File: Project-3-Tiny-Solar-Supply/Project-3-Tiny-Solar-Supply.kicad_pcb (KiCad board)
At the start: 2 copper layers, 40.8 x 18.5 mm, 16 parts, among them J1 Conn_01x02_Pin, J2 Conn_01x02_Pin, J3 Conn_01x02_Pin, J4 Conn_01x02_Pin, Q1 2N7002, U1 AP3015AKTR-G1

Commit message: rotate diodes
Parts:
- turned D1 to 180 degrees
- turned D2 to 180 degrees
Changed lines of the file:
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@@
 	(footprint "SS14:DO-214AC"
 		(layer "F.Cu")
-		(at 58.75 86)
+		(at 58.75 86 180)
 		(property "Reference" "D1"
-			(at 4.05 0.1 0)
+			(at -4.15 0.1 0)
 			(layer "F.SilkS")
 			(effects
@@
 		(duplicate_pad_numbers_are_jumpers no)
 		(fp_line
+			(start 2.3 1.2)
+			(end -2.3 1.2)
+			(stroke
+				(width 0.15)
+				(type solid)
+			)
+			(layer "F.SilkS")
+		)
+		(fp_line
+			(start 0.25 0.7)
+			(end -0.8 0)
+			(stroke
+				(width 0.15)
+				(type solid)
+			)
+			(layer "F.SilkS")
+		)
+		(fp_line
+			(start 0.25 -0.75)
+			(end 0.25 0.7)
+			(stroke
+				(width 0.15)
+				(type solid)
+			)
+			(layer "F.SilkS")
+		)
+		(fp_line
+			(start -0.8 0)
+			(end 0.25 -0.75)
+			(stroke
+				(width 0.15)
+				(type solid)
+			)
+			(layer "F.SilkS")
+		)
+		(fp_line
 			(start -2.3 -1.2)
 			(end 2.3 -1.2)
-			(stroke
-				(width 0.15)
-				(type solid)
-			)
-			(layer "F.SilkS")
-		)
-		(fp_line
-			(start -0.8 0)
-			(end 0.25 -0.75)
-			(stroke
-				(width 0.15)
-				(type solid)
-			)
-			(layer "F.SilkS")
-		)
-		(fp_line
-			(start 0.25 -0.75)
-			(end 0.25 0.7)
-			(stroke
-				(width 0.15)
-				(type solid)
-			)
-			(layer "F.SilkS")
-		)
-		(fp_line
-			(start 0.25 0.7)
-			(end -0.8 0)
-			(stroke
-				(width 0.15)
-				(type solid)
-			)
-			(layer "F.SilkS")
-		)
-		(fp_line
-			(start 2.3 1.2)
-			(end -2.3 1.2)
 			(stroke
 				(width 0.15)
@@
 		)
 		(fp_line
+			(start 2.3 -1.2)
+			(end 2.3 1.2)
+			(stroke
+				(width 0.15)
+				(type solid)
+			)
+			(layer "F.Fab")
+		)
+		(fp_line
 			(start -2.3 1.2)
 			(end -2.3 -1.2)
@@
 			(layer "F.Fab")
 		)
-		(fp_line
-			(start 2.3 -1.2)
-			(end 2.3 1.2)
-			(stroke
-				(width 0.15)
-				(type solid)
-			)
+		(fp_poly
+			(pts
+				(xy 2.35 -0.65) (xy 2.6 -0.65) (xy 2.6 0.7) (xy 2.35 0.7)
+			)
+			(stroke
+				(width 0.01)
+				(type solid)
+			)
+			(fill yes)
 			(layer "F.Fab")
 		)
@@
 			(layer "F.Fab")
 		)
-		(fp_poly
-			(pts
-				(xy 2.35 -0.65) (xy 2.6 -0.65) (xy 2.6 0.7) (xy 2.35 0.7)
-			)
-			(stroke
-				(width 0.01)
-				(type solid)
-			)
-			(fill yes)
-			(layer "F.Fab")
-		)
 		(pad "A" smd rect
-			(at 2.05 0)
+			(at 2.05 0 180)
 			(size 1.8 1.7)
 			(layers "F.Cu" "F.Mask" "F.Paste")
@@
 		)
 		(pad "K" smd rect
-			(at -2.05 0)
+			(at -2.05 0 180)
 			(size 1.8 1.7)
 			(layers "F.Cu" "F.Mask" "F.Paste")
@@
 	(footprint "SS14:DO-214AC"
 		(layer "F.Cu")
-		(at 49.5 86)
+		(at 49.5 86 180)
 		(property "Reference" "D2"
-			(at 4.1 0.1 0)
+			(at -4.1 0.1 0)
 			(layer "F.SilkS")
 			(effects
@@
 		(duplicate_pad_numbers_are_jumpers no)
 		(fp_line
+			(start 2.3 1.2)
+			(end -2.3 1.2)
+			(stroke
+				(width 0.15)
+				(type solid)
+			)
+			(layer "F.SilkS")
+		)
+		(fp_line
+			(start 0.25 0.7)
+			(end -0.8 0)
+			(stroke
+				(width 0.15)
+				(type solid)
+			)
+			(layer "F.SilkS")
+		)
+		(fp_line
+			(start 0.25 -0.75)
+			(end 0.25 0.7)
+			(stroke
+				(width 0.15)
+				(type solid)
+			)
+			(layer "F.SilkS")
+		)
+		(fp_line
+			(start -0.8 0)
+			(end 0.25 -0.75)
+			(stroke
+				(width 0.15)
+				(type solid)
+			)
+			(layer "F.SilkS")
+		)
+		(fp_line
 			(start -2.3 -1.2)
 			(end 2.3 -1.2)
-			(stroke
-				(width 0.15)
-				(type solid)
-			)
-			(layer "F.SilkS")
-		)
-		(fp_line
-			(start -0.8 0)
-			(end 0.25 -0.75)
-			(stroke
-				(width 0.15)
-				(type solid)
-			)
-			(layer "F.SilkS")
-		)
-		(fp_line
-			(start 0.25 -0.75)
-			(end 0.25 0.7)
-			(stroke
-				(width 0.15)
-				(type solid)
-			)
-			(layer "F.SilkS")
-		)
-		(fp_line
-			(start 0.25 0.7)
-			(end -0.8 0)
-			(stroke
-				(width 0.15)
-				(type solid)
-			)
-			(layer "F.SilkS")
-		)
-		(fp_line
-			(start 2.3 1.2)
-			(end -2.3 1.2)
 			(stroke
 				(width 0.15)
@@
 		)
 		(fp_line
+			(start 2.3 -1.2)
+			(end 2.3 1.2)
+			(stroke
+				(width 0.15)
+				(type solid)
+			)
+			(layer "F.Fab")
+		)
+		(fp_line
 			(start -2.3 1.2)
 			(end -2.3 -1.2)
@@
 			(layer "F.Fab")
 		)
-		(fp_line
-			(start 2.3 -1.2)
-			(end 2.3 1.2)
-			(stroke
-				(width 0.15)
-				(type solid)
-			)
+		(fp_poly
+			(pts
+				(xy 2.35 -0.65) (xy 2.6 -0.65) (xy 2.6 0.7) (xy 2.35 0.7)
+			)
+			(stroke
+				(width 0.01)
+				(type solid)
+			)
+			(fill yes)
 			(layer "F.Fab")
 		)
@@
 			(layer "F.Fab")
 		)
-		(fp_poly
-			(pts
-				(xy 2.35 -0.65) (xy 2.6 -0.65) (xy 2.6 0.7) (xy 2.35 0.7)
-			)
-			(stroke
-				(width 0.01)
-				(type solid)
-			)
-			(fill yes)
-			(layer "F.Fab")
-		)
 		(pad "A" smd rect
-			(at 2.05 0)
+			(at 2.05 0 180)
 			(size 1.8 1.7)
 			(layers "F.Cu" "F.Mask" "F.Paste")
@@
 		)
 		(pad "K" smd rect
-			(at -2.05 0)
+			(at -2.05 0 180)
 			(size 1.8 1.7)
 			(layers "F.Cu" "F.Mask" "F.Paste")

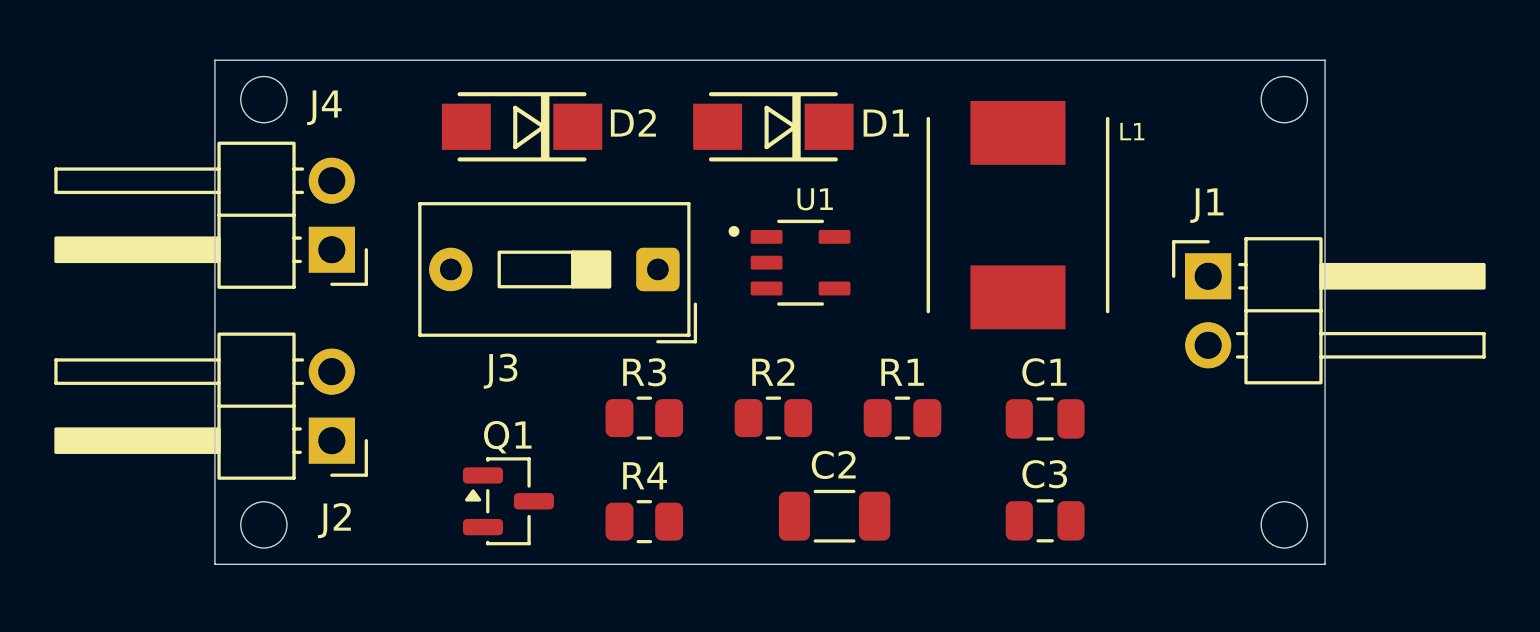
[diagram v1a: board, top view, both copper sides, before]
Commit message: re-arrange and wire footprints (GND plane missing)
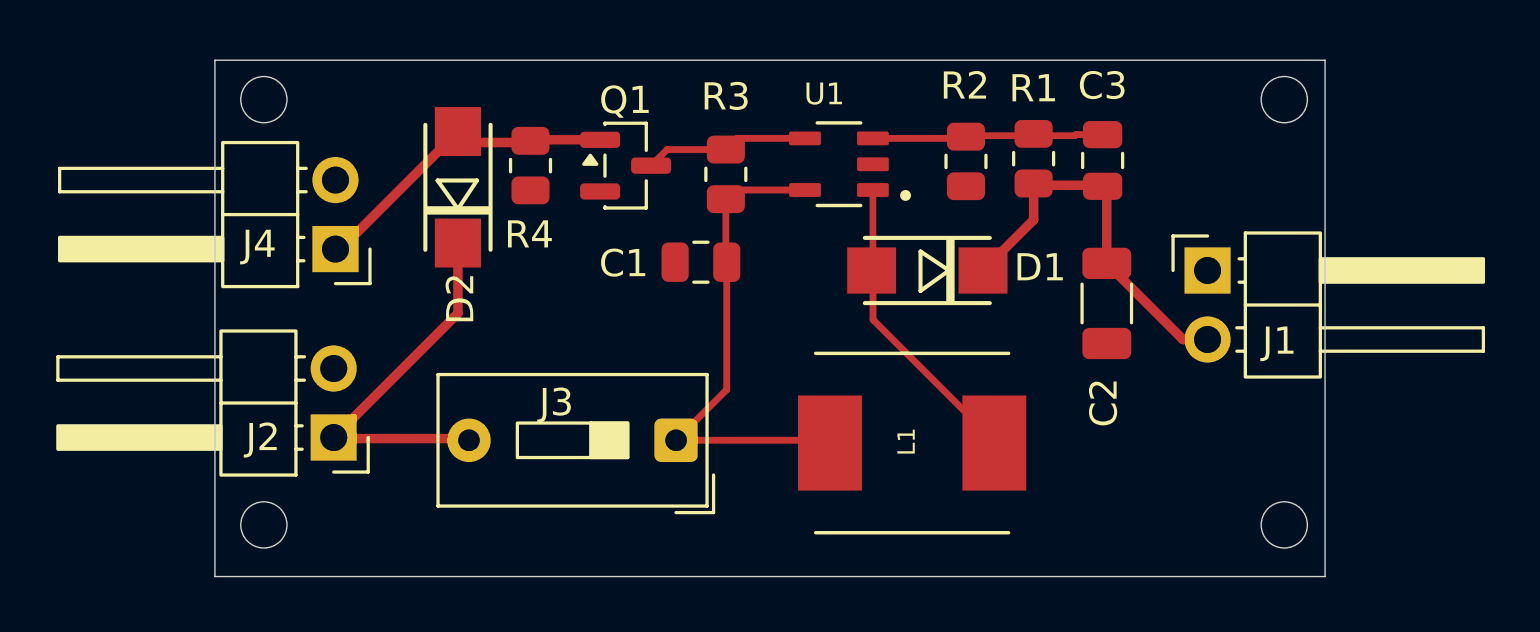
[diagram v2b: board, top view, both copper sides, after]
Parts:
- moved C1 13.9 mm to (56.1, 91.0), turned to 180 degrees
- moved R4 13.8 mm to (49.8, 87.4), turned to -90 degrees
- moved C3 13.4 mm to (70.9, 87.2), turned to 90 degrees
- moved Q1 13.1 mm to (53.3, 87.4)
- moved C2 12.7 mm to (71.0, 92.5), turned to -90 degrees
- moved R2 11.8 mm to (65.8, 87.3), turned to -90 degrees
- moved R1 10.7 mm to (68.3, 87.2), turned to 90 degrees
- moved R3 9.46 mm to (57.0, 87.8), turned to 90 degrees
- moved L1 9.25 mm to (63.9, 97.6), turned to 0 degrees
- moved D1 7.75 mm to (64.4, 91.3)
- moved J3 6.32 mm to (55.2, 97.5)
- moved U1 3.89 mm to (61.2, 87.4), turned to 180 degrees
- moved D2 3.24 mm to (47.1, 88.2), turned to 90 degrees
- moved J1 0.21 mm to (74.7, 91.3)
- moved J4 0.14 mm to (42.6, 90.5)
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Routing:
- net Net-(J3-Pin_1): track 0.00 -> 18.0 mm
- net /OUT_P: track 0.00 -> 14.8 mm
- net /BAT_P: track 0.00 -> 14.1 mm
- net /SOLAR_P: track 0.00 -> 11.9 mm
- net Net-(D1-A): track 0.00 -> 11.5 mm
- net Net-(U1-FB): track 0.00 -> 8.51 mm
- net Net-(Q1-D): track 0.00 -> 6.22 mm
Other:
- board size 40.8 x 18.5 mm -> 40.8 x 19 mm

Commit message: fine re-arrange and wiring, clean up
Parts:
- moved J1 1.25 mm to (73.5, 91.5)
- moved C2 1.02 mm to (70.0, 92.5)
- moved C1 0.77 mm to (56.0, 91.8)
- moved R3 0.53 mm to (57.0, 87.2)
- moved D1 0.41 mm to (64.0, 91.3)
- moved R2 0.37 mm to (65.5, 87.2)
- moved R1 0.37 mm to (68.0, 87.2)
- moved C3 0.37 mm to (70.5, 87.2)
- moved D2 0.24 mm to (47.1, 88.5)
- moved R4 0.21 mm to (49.8, 87.2)
- moved Q1 0.19 mm to (53.3, 87.2)
- moved U1 0.13 mm to (61.2, 87.2)
- moved L1 0.11 mm to (63.8, 97.6)
- moved J2 0.09 mm to (42.6, 97.5)
- moved J3 0.09 mm to (55.2, 97.6)
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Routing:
- net Net-(D1-A): track 11.5 -> 3.28 mm
- net /OUT_P: track 14.8 -> 14.3 mm
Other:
- board size 40.8 x 19 mm -> 39.7 x 18.5 mm

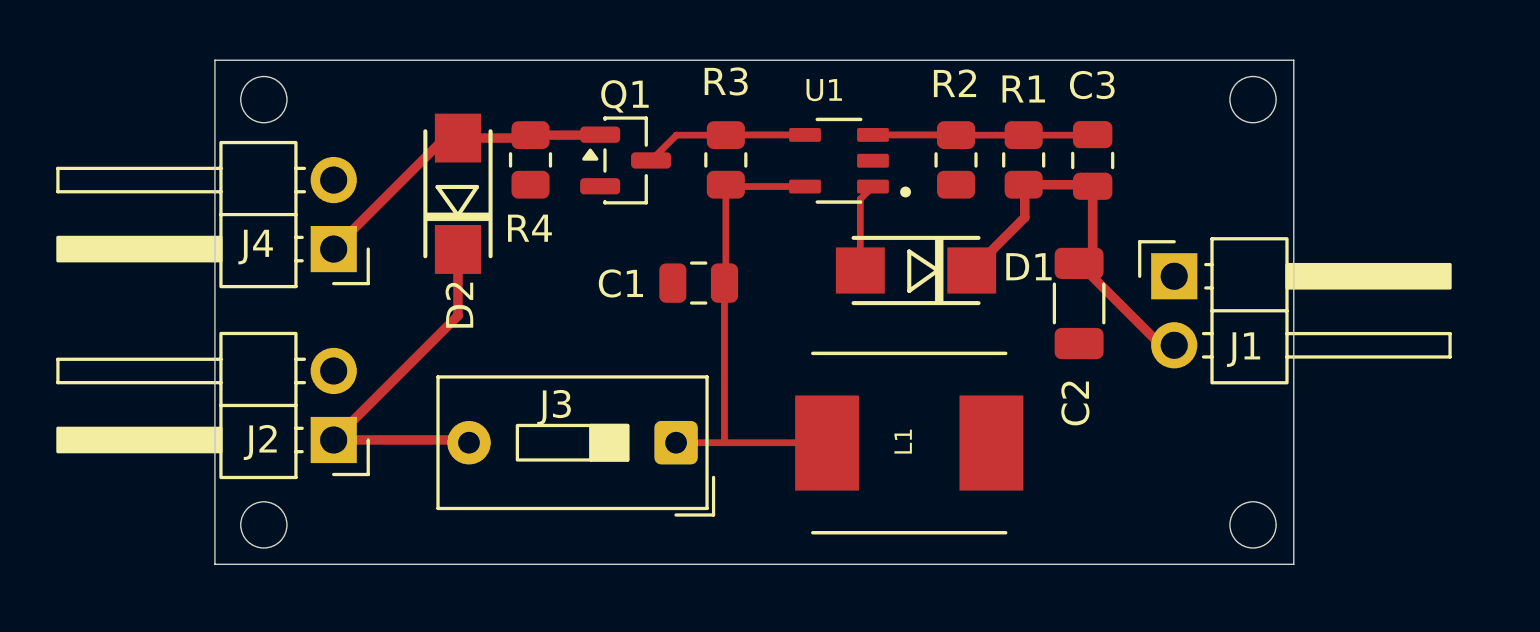
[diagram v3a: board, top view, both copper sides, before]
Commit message: add back copper fill for GNDD plane
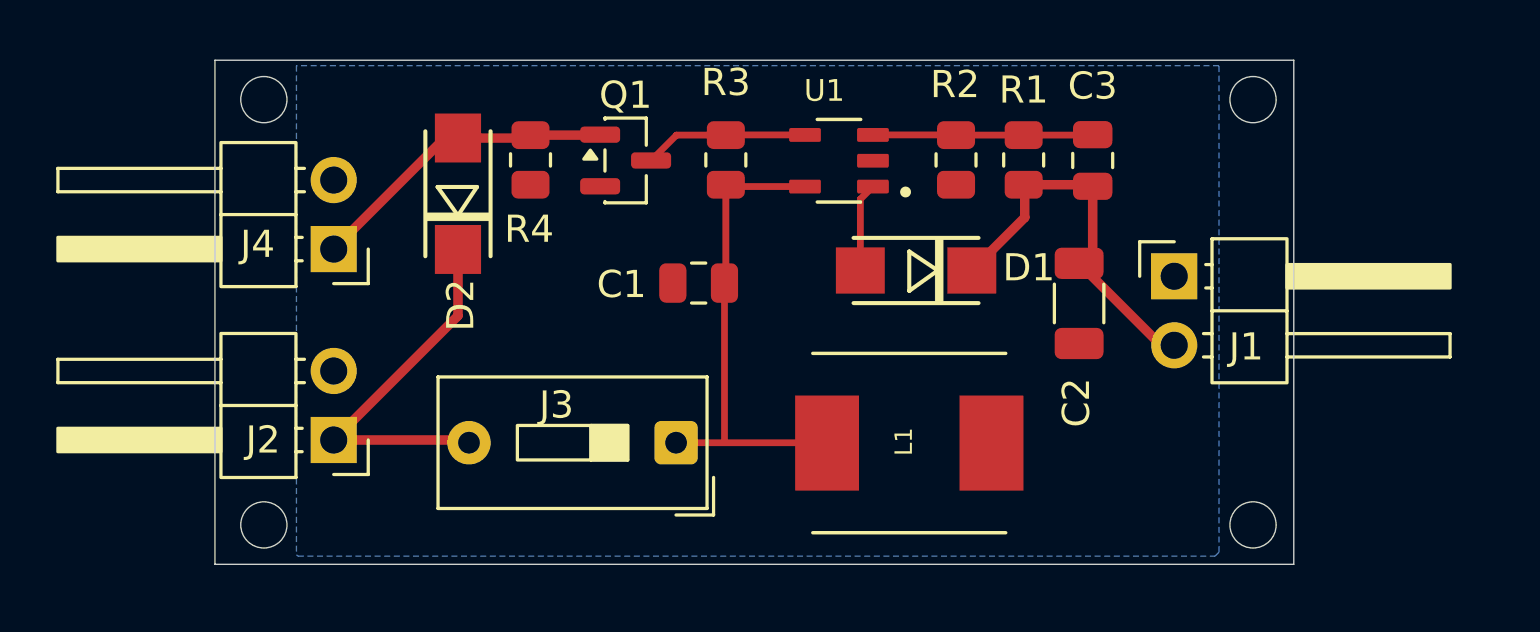
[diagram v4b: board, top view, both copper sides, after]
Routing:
- added copper zone on B.Cu, net GNDD
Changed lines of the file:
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@@
 		(net "/BAT_P")
+	)
+	(zone
+		(net "GNDD")
+		(layer "B.Cu")
+		(name "GNDD_zone")
+		(hatch edge 0.5)
+		(connect_pads
+			(clearance 0.5)
+		)
+		(min_thickness 0.25)
+		(fill
+			(mode hatch)
+			(thermal_gap 0.5)
+			(thermal_bridge_width 0.5)
+			(island_removal_mode 0)
+			(hatch_thickness 1)
+			(hatch_gap 1.5)
+			(hatch_orientation 0)
+			(hatch_border_algorithm hatch_thickness)
+			(hatch_min_hole_area 0.15)
+		)
+		(polygon
+			(pts
+				(xy 41.2 83.75) (xy 41.2 101.75) (xy 41.25 101.8) (xy 75 101.8) (xy 75.15 101.65) (xy 75.15 83.75)
+			)
+		)
 	)
 	(embedded_fonts no)

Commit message: bugfix, add again the missing connection L1.pin2-to-D1.pin2
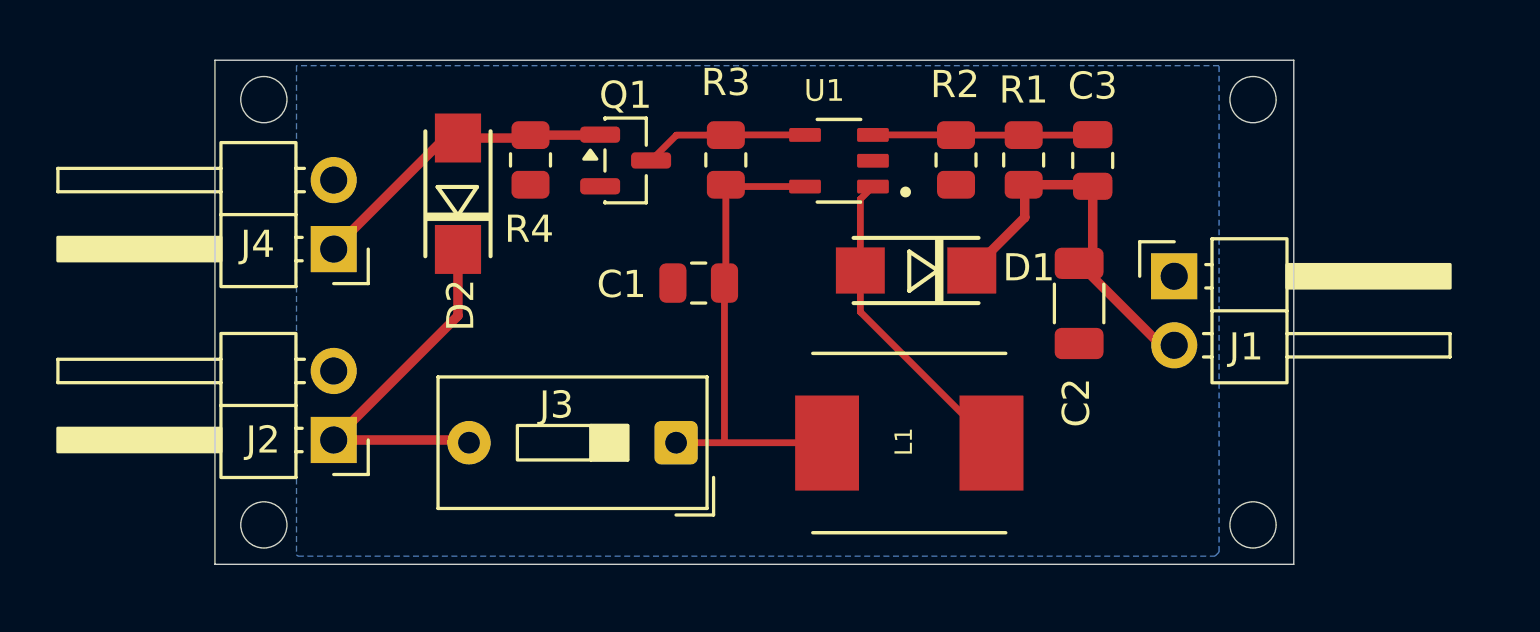
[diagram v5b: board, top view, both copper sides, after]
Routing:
- net Net-(D1-A): track 3.28 -> 11.6 mm
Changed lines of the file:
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@@
 		(capping no)
 		(filling no)
+		(zone_defaults)
 		(pcbplotparams
 			(layerselection 0x00000000_00000000_55555555_5755f5ff)
@@
 	)
 	(segment
+		(start 61.95 92.8126)
+		(end 66.775 97.6376)
+		(width 0.25)
+		(layer "F.Cu")
+		(net "Net-(D1-A)")
+	)
+	(segment
+		(start 61.95 91.2876)
+		(end 61.95 92.8126)
+		(width 0.25)
+		(layer "F.Cu")
+		(net "Net-(D1-A)")
+	)
+	(segment
 		(start 61.95 88.662)
 		(end 61.95 91.2876)
@@
 		)
 		(min_thickness 0.25)
-		(fill
+		(fill yes
 			(mode hatch)
 			(thermal_gap 0.5)
